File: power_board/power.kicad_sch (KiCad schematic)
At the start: 21 parts, among them U6 LM5163DDAR, U7 LP2985-33DBVR, U8 LP2985-33DBVR

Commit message: Complete sch design without check
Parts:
- added C30, C31: 1u, symbol Device:C_Small
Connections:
- net GND: now also C30.2, C31.2
- net at C27.1, R41.2, U8.1 (VIN)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: now also C31.1
- net at C24.1, R40.2, U7.1 (VIN)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: now also C30.1

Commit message: Start multichannel layout
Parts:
- removed U7, U8: LP2985-33DBVR, esc-library:SOT-23-5_L2.9-W1.6-P0.95-LS2.8-TL, symbol esc-library:LP2985-33DBVR
- added D7: LED, LED_SMD:LED_0603_1608Metric, symbol Device:LED
- added R40: 2.2k, Resistor_SMD:R_0603_1608Metric, symbol Device:R_Small
- added U12, U13: LP2985-33DBVR, esc-library:SOT-23-5_L3.0-W1.7-P0.95-LS2.8-BR, symbol esc-library:LP2985-33DBVR
- C25: renamed from C19; footprint (none) -> Capacitor_SMD:C_0603_1608Metric
- C26: renamed from C24; footprint (none) -> Capacitor_SMD:C_0603_1608Metric
- C27: footprint (none) -> Capacitor_SMD:C_0603_1608Metric
- C28: renamed from C30; footprint (none) -> Capacitor_SMD:C_0603_1608Metric
- C29: renamed from C31; footprint (none) -> Capacitor_SMD:C_0603_1608Metric
- C30: renamed from C20; footprint (none) -> Capacitor_SMD:C_0603_1608Metric
- C31: renamed from C21; footprint (none) -> Capacitor_SMD:C_0603_1608Metric
- C32: renamed from C25; footprint (none) -> Capacitor_SMD:C_0603_1608Metric
- C33: renamed from C28; footprint (none) -> Capacitor_SMD:C_0603_1608Metric
- C34: renamed from C22; footprint (none) -> Capacitor_SMD:C_0603_1608Metric
- C35: renamed from C23; footprint (none) -> Capacitor_SMD:C_0603_1608Metric
- C36: renamed from C26; footprint (none) -> Capacitor_SMD:C_0603_1608Metric
- C37: renamed from C29; footprint (none) -> Capacitor_SMD:C_0603_1608Metric
- R34: renamed from R40; footprint (none) -> Resistor_SMD:R_0603_1608Metric
- R35: renamed from R41; footprint (none) -> Resistor_SMD:R_0603_1608Metric
- R36, R37, R38, R39: footprint (none) -> Resistor_SMD:R_0603_1608Metric
- renumbered U6 to U11
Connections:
- net +12V: now also R40.1
- net +3V3: now also U13.5 (VOUT)
- net +3V3A: now also U12.5 (VOUT)
- net GND: now also U12.2 (GND), U13.2 (GND)
- net at C27.1, C29.1, R35.2: now also U13.1 (VIN), U13.3 (ON/~{OFF})
- net at C32.1: now also U12.4 (BYPASS)
- net at C26.1, C28.1, R34.2: now also U12.1 (VIN), U12.3 (ON/~{OFF})
- net at C33.1: now also U13.4 (BYPASS)
- net PG: now reaches U11.6 (PGOOD)
- net PG: now also D7.1 (K)
- new net: D7.2 (A), R40.2
- no-connect marks 1 -> 0

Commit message: Complete primary layout step
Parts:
- added C39, C40: 1u, Capacitor_SMD:C_0603_1608Metric, symbol Device:C_Small
- added C41: 10n, Capacitor_SMD:C_0603_1608Metric, symbol Device:C_Small
- added C42: 2.2u, Capacitor_SMD:C_0603_1608Metric, symbol Device:C_Small
- added R41: 2.2, Resistor_SMD:R_0603_1608Metric, symbol Device:R_Small
- added U12: LP2985-33DBVR, esc-library:SOT-23-5_L3.0-W1.7-P0.95-LS2.8-BR, symbol esc-library:LP2985-33DBVR
- C34: renamed from C35; footprint Capacitor_SMD:C_0603_1608Metric -> Capacitor_SMD:C_1210_3225Metric
- R36: value R_Small -> 100k
- R39: value 49.9 -> 49.9k
- renumbered C25 to C24, C26 to C25, C27 to C26, C28 to C27, C29 to C28, C30 to C29, C31 to C30, C32 to C31, C33 to C32, C34 to C33, C36 to C35, C37 to C36, U12 to U10, U13 to U11, U11 to U9
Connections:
- net +12V: now also R41.1
- net GND: now also C39.2, C40.2, C41.2, C42.2, U12.2 (GND)
- net at L1.1, R37.2: now also C29.1, U9.8 (SW); no longer C29.2, U9.7 (BST)
- new net: C41.1, U12.4 (BYPASS)
- new net: C39.1, C40.1, R41.2, U12.1 (VIN), U12.3 (ON/~{OFF})
- new net: C29.2, U9.7 (BST)
- new net +3V3A0: C42.1, U12.5 (VOUT)

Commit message: All drc error solved
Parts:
- added C43: 22u, Capacitor_SMD:C_1210_3225Metric, symbol Device:C_Small
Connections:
- net +12V: now also C43.1
- net GND: no longer C24.2, C25.2, C26.2, C34.2, C39.2, R36.1, R39.2, U9.1 (GND), U9.9 (EP)
- new net VSS: C24.2, C25.2, C26.2, C34.2, C39.2, C43.2, R36.1, R39.2, U9.1 (GND), U9.9 (EP)

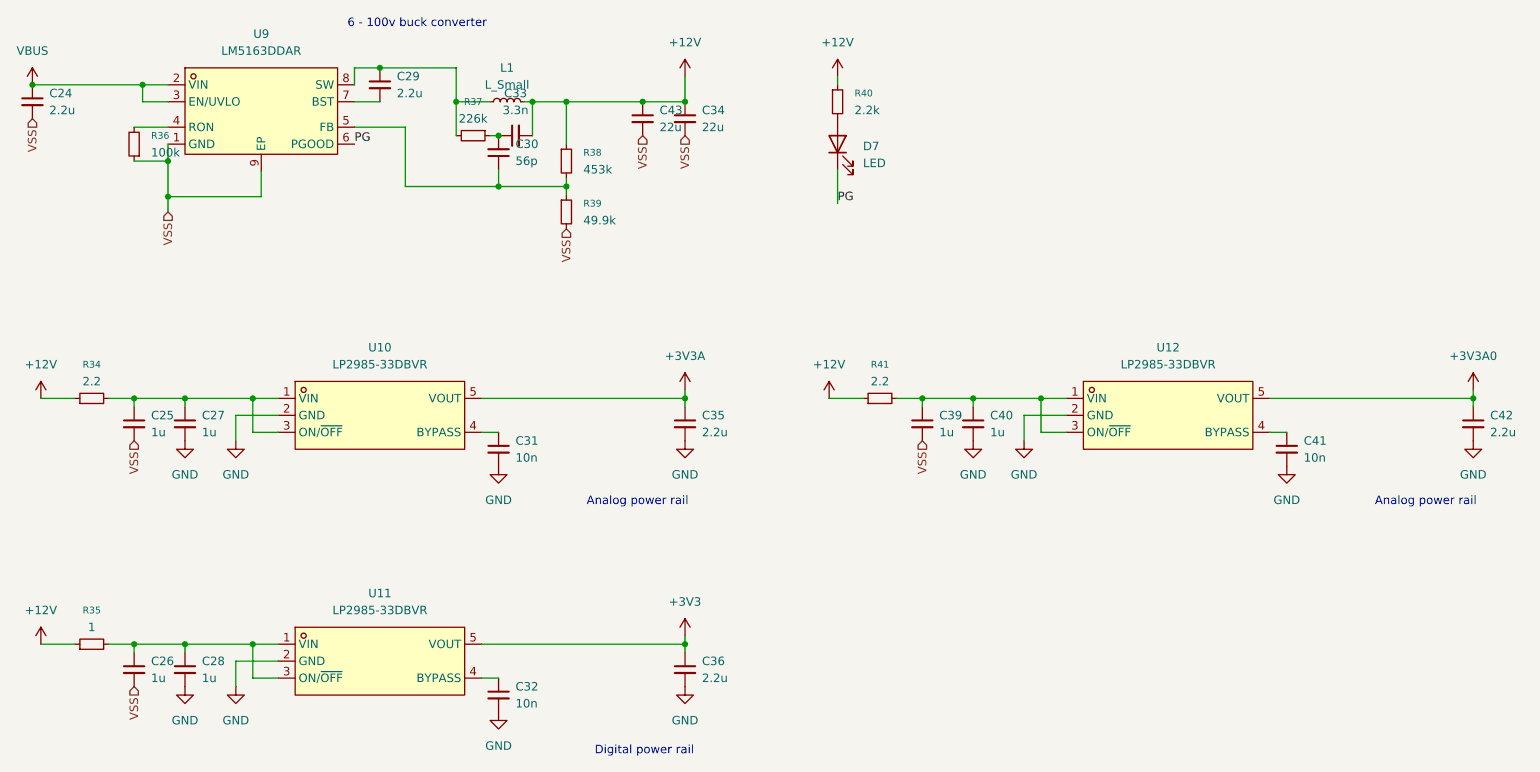
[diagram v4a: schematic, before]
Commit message: Add testpoint, SWD, and PWM port
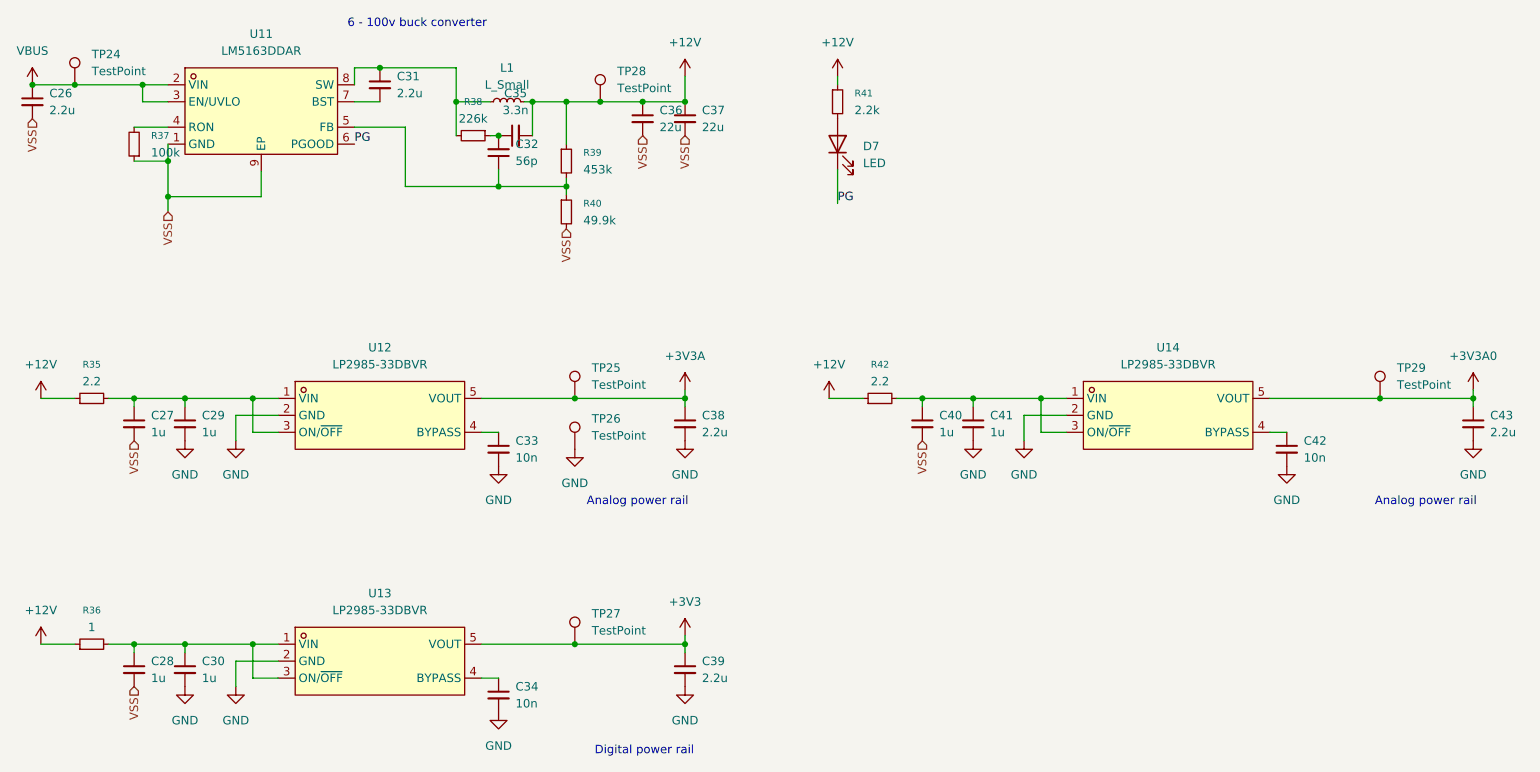
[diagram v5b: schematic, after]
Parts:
- added TP24, TP25, TP26, TP27, TP28, TP29: TestPoint, esc-library:SMD_RH-5015, symbol Connector:TestPoint
- renumbered C24 to C26, C25 to C27, C26 to C28, C27 to C29, C28 to C30, C29 to C31, C30 to C32, C31 to C33, C32 to C34, C33 to C35, C43 to C36, C34 to C37, C35 to C38, C36 to C39, C39 to C40, C40 to C41, C41 to C42, C42 to C43, R34 to R35, R35 to R36, R36 to R37, R37 to R38, R38 to R39, R39 to R40, R40 to R41, R41 to R42, U9 to U11, U10 to U12, U11 to U13, U12 to U14
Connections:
- net +12V: now also TP28.1
- net +3V3: now also TP27.1
- net +3V3A: now also TP25.1
- net +3V3A0: now also TP29.1
- net GND: now also TP26.1
- net VBUS: now also TP24.1

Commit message: Complete all design, pass DRC
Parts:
- added TP32, TP33: GND, esc-library:SMD_RH-5015, symbol Connector:TestPoint
- added TP34: TestPoint, esc-library:SMD_RH-5015, symbol Connector:TestPoint
- L1: value L_Small -> 100u
- TP24: value TestPoint -> VBUS_IN
- TP25: value TestPoint -> 3V3A
- TP26: value TestPoint -> GND
- TP27: value TestPoint -> 3V3
- TP28: value TestPoint -> 12V
- TP29: value TestPoint -> 3V3A0
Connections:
- net GND: now also TP32.1, TP33.1
- net VSS: now also TP34.1
